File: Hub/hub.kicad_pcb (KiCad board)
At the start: 2 copper layers, 45 parts, among them J1 Barrel_Jack, J2 Conn_01x06_Male, U1 PIC32MX575F512H-80I_PT, U2 AT86RF231-ZU, U3 TPS56339DDC, U4 TPS56339DDC

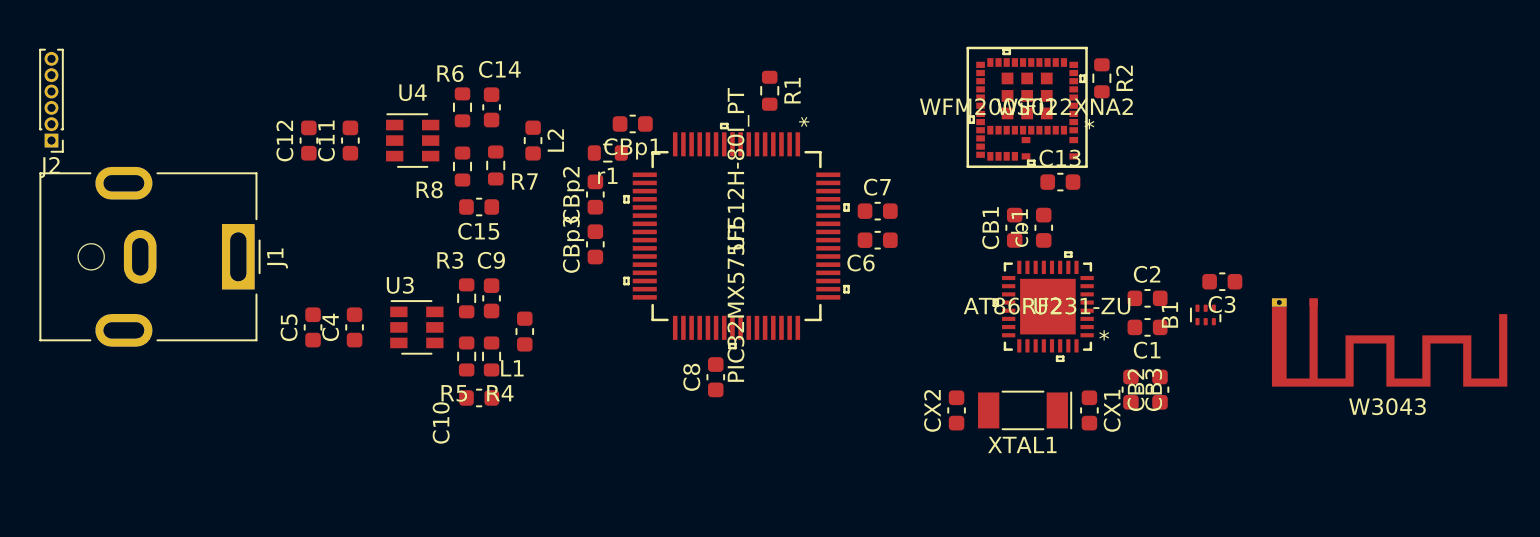
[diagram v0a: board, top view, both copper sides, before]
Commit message: hub pcb routed
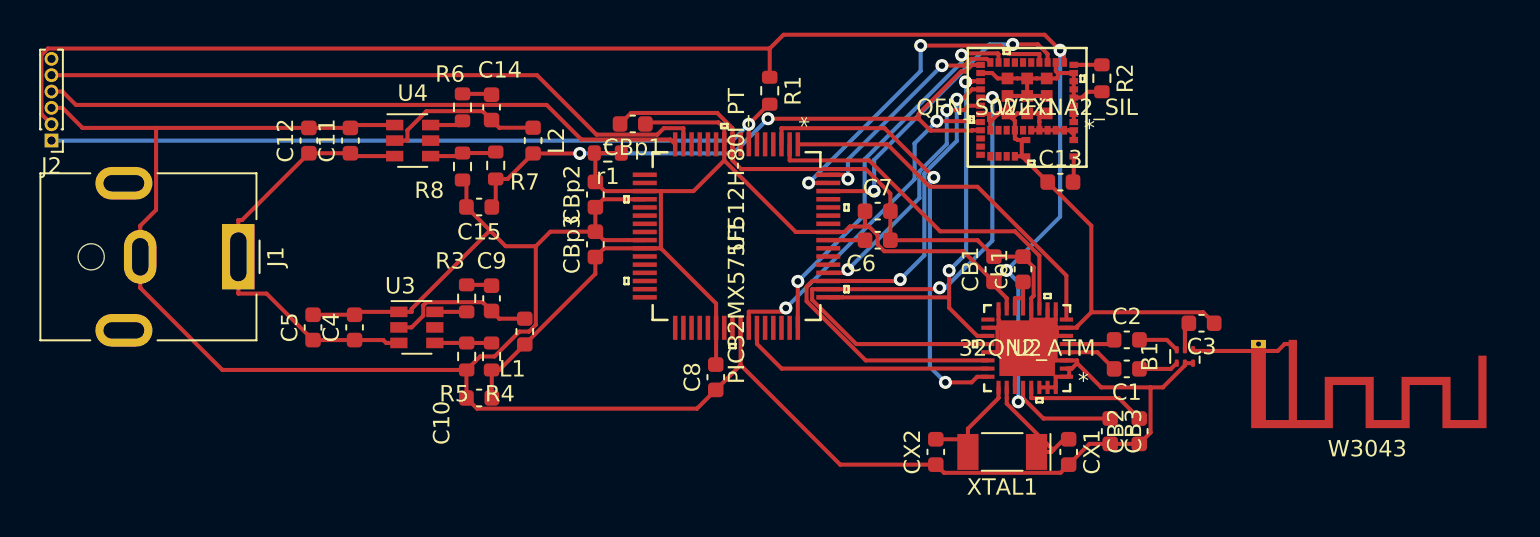
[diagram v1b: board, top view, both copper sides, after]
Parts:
- U1: footprint MCU_HUB:PIC32MX575F512H-80I&slash_PT -> funcMCU:PIC32MX575F512H-80I&slash_PT
- U2: value AT86RF231-ZU -> 32QN2_ATM; footprint ZBEE:AT86RF231-ZU -> funcZB:AT86RF231-ZU
- WiFi1: value WFM200S022XNA2 -> QFN_S022XNA2_SIL; footprint WIFI:WFM200S022XNA2 -> funcWIFI:WFM200S022XNA2
- moved C1 2.84 mm to (115.3, 66.5)
- moved CB2 2.84 mm to (116.1, 70.4)
- moved CB3 2.84 mm to (114.3, 70.4)
- moved CX1 2.84 mm to (111.8, 71.6)
- moved CX2 2.84 mm to (103.6, 71.6)
- moved U2 2.84 mm to (109.2, 65.3)
- moved XTAL1 2.84 mm to (107.7, 71.6)
- moved cb1 2.84 mm to (109.0, 60.5)
- moved B1 2.84 mm to (118.9, 65.8)
- moved C2 2.84 mm to (115.3, 64.8)
- moved C3 2.84 mm to (119.9, 63.8)
- moved CB1 2.84 mm to (107.2, 60.5)
- moved W3043 2.84 mm to (125.5, 65.0)
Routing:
- net GND: track 0.00 -> 265.2 mm
- net +3V3: track 0.00 -> 171.6 mm, vias 0 -> 3
- net MCLR: track 0.00 -> 46.1 mm, vias 0 -> 1
- net PGC: track 0.00 -> 41.3 mm
- net PGD: track 0.00 -> 39.5 mm
- net +1V8: track 0.00 -> 38.6 mm, vias 0 -> 2
- net SPI_MISO: track 0.00 -> 34.3 mm, vias 0 -> 2
- net SPI_MOSI: track 0.00 -> 33.6 mm, vias 0 -> 2
- net IRQ_ZGB: track 0.00 -> 27.3 mm, vias 0 -> 2
- net VCC: track 0.00 -> 26.9 mm
- net SPI_CLK: track 0.00 -> 25.7 mm, vias 0 -> 2
- net LP_CLK: track 0.00 -> 23.7 mm, vias 0 -> 2
- net RESET_ZGB: track 0.00 -> 22.4 mm
- net SLP_TR: track 0.00 -> 21.9 mm
- net SPI_CS2: track 0.00 -> 21.3 mm, vias 0 -> 2
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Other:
- net class Default: clearance 0.2 -> 0.05
- rule trace_clearance: 0.2 -> 0.05
